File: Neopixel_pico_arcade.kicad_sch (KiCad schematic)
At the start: 14 parts

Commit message: Adds a buzzer to the schematics
We needed a way to generate some kind of annoying sound :)
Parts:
- added Q?: 2N7002, Package_TO_SOT_SMD:SOT-23, symbol Transistor_FET:2N7002
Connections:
- net +5V: now also BZ?.1 (-)
- net BUZZ: now also Q?.1 (G); no longer BZ?.1 (-)
- net GND: now also Q?.2 (S); no longer BZ?.2 (+)
- new net: BZ?.2 (+), Q?.3 (D)
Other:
- moved on the sheet: BZ?
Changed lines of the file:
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@@
     (stroke (width 0) (type solid) (color 0 0 0 0))
   )
-  (wire (pts (xy 233.68 38.1) (xy 237.49 38.1))
+  (wire (pts (xy 212.09 46.99) (xy 215.9 46.99))
     (stroke (width 0) (type default) (color 0 0 0 0))
   )
-  (wire (pts (xy 236.22 43.18) (xy 236.22 45.72))
+  (wire (pts (xy 223.52 25.4) (xy 223.52 30.48))
     (stroke (width 0) (type default) (color 0 0 0 0))
   )
-  (wire (pts (xy 237.49 43.18) (xy 236.22 43.18))
+  (wire (pts (xy 223.52 30.48) (xy 224.79 30.48))
+    (stroke (width 0) (type default) (color 0 0 0 0))
+  )
+  (wire (pts (xy 223.52 35.56) (xy 223.52 41.91))
+    (stroke (width 0) (type default) (color 0 0 0 0))
+  )
+  (wire (pts (xy 223.52 52.07) (xy 223.52 55.88))
+    (stroke (width 0) (type default) (color 0 0 0 0))
+  )
+  (wire (pts (xy 224.79 35.56) (xy 223.52 35.56))
     (stroke (width 0) (type default) (color 0 0 0 0))
   )
@@
     )
   )
-  (global_label "BUZZ" (shape input) (at 233.68 38.1 180) (fields_autoplaced)
+  (global_label "BUZZ" (shape input) (at 212.09 46.99 180) (fields_autoplaced)
     (effects (font (size 1.27 1.27)) (justify right))
-    (property "Intersheet References" "${INTERSHEET_REFS}" (id 0) (at 226.2474 38.1794 0)
+    (property "Intersheet References" "${INTERSHEET_REFS}" (id 0) (at 204.6574 47.0694 0)
       (effects (font (size 1.27 1.27)) (justify right) hide)
     )
@@
     (pin "1")
   )
+  (symbol (lib_id "Generative_picture:+5V_USB") (at 223.52 25.4 0) (unit 1)
+    (in_bom yes) (on_board yes)
+    (property "Reference" "#PWR?" (id 0) (at 223.52 29.21 0)
+      (effects (font (size 1.27 1.27)) hide)
+    )
+    (property "Value" "+5V" (id 1) (at 223.8883 21.0756 0))
+    (property "Footprint" "" (id 2) (at 223.52 25.4 0)
+      (effects (font (size 1.27 1.27)) hide)
+    )
+    (property "Datasheet" "" (id 3) (at 223.52 25.4 0)
+      (effects (font (size 1.27 1.27)) hide)
+    )
+    (pin "1")
+  )
   (symbol (lib_id "Generative_picture:+5V_USB") (at 240.665 64.77 0) (unit 1)
     (in_bom yes) (on_board yes)
@@
     (pin "1")
   )
-  (symbol (lib_id "power:GND") (at 236.22 45.72 0) (mirror y) (unit 1)
-    (in_bom yes) (on_board yes)
-    (property "Reference" "#PWR?" (id 0) (at 236.22 52.07 0)
-      (effects (font (size 1.27 1.27)) hide)
-    )
-    (property "Value" "GND" (id 1) (at 236.1057 50.0444 0))
-    (property "Footprint" "" (id 2) (at 236.22 45.72 0)
-      (effects (font (size 1.27 1.27)) hide)
-    )
-    (property "Datasheet" "" (id 3) (at 236.22 45.72 0)
+  (symbol (lib_id "power:GND") (at 223.52 55.88 0) (mirror y) (unit 1)
+    (in_bom yes) (on_board yes)
+    (property "Reference" "#PWR?" (id 0) (at 223.52 62.23 0)
+      (effects (font (size 1.27 1.27)) hide)
+    )
+    (property "Value" "GND" (id 1) (at 223.4057 60.2044 0))
+    (property "Footprint" "" (id 2) (at 223.52 55.88 0)
+      (effects (font (size 1.27 1.27)) hide)
+    )
+    (property "Datasheet" "" (id 3) (at 223.52 55.88 0)
       (effects (font (size 1.27 1.27)) hide)
     )
@@
     (pin "3")
   )
-  (symbol (lib_id "Device:Buzzer") (at 240.03 40.64 0) (unit 1)
+  (symbol (lib_id "Device:Buzzer") (at 227.33 33.02 0) (unit 1)
     (in_bom yes) (on_board yes) (fields_autoplaced)
-    (property "Reference" "BZ?" (id 0) (at 243.8401 39.7315 0)
+    (property "Reference" "BZ?" (id 0) (at 231.1401 32.1115 0)
       (effects (font (size 1.27 1.27)) (justify left))
     )
-    (property "Value" "Buzzer" (id 1) (at 243.8401 42.5066 0)
+    (property "Value" "Buzzer" (id 1) (at 231.1401 34.8866 0)
       (effects (font (size 1.27 1.27)) (justify left))
     )
-    (property "Footprint" "" (id 2) (at 239.395 38.1 90)
-      (effects (font (size 1.27 1.27)) hide)
-    )
-    (property "Datasheet" "~" (id 3) (at 239.395 38.1 90)
+    (property "Footprint" "" (id 2) (at 226.695 30.48 90)
+      (effects (font (size 1.27 1.27)) hide)
+    )
+    (property "Datasheet" "~" (id 3) (at 226.695 30.48 90)
       (effects (font (size 1.27 1.27)) hide)
     )
@@
     (pin "6")
     (pin "7")
+  )
+  (symbol (lib_id "Transistor_FET:2N7002") (at 220.98 46.99 0) (unit 1)
+    (in_bom yes) (on_board yes) (fields_autoplaced)
+    (property "Reference" "Q?" (id 0) (at 226.1871 46.0815 0)
+      (effects (font (size 1.27 1.27)) (justify left))
+    )
+    (property "Value" "2N7002" (id 1) (at 226.1871 48.8566 0)
+      (effects (font (size 1.27 1.27)) (justify left))
+    )
+    (property "Footprint" "Package_TO_SOT_SMD:SOT-23" (id 2) (at 226.06 48.895 0)
+      (effects (font (size 1.27 1.27) italic) (justify left) hide)
+    )
+    (property "Datasheet" "https://www.onsemi.com/pub/Collateral/NDS7002A-D.PDF" (id 3) (at 220.98 46.99 0)
+      (effects (font (size 1.27 1.27)) (justify left) hide)
+    )
+    (pin "1")
+    (pin "2")
+    (pin "3")
   )
   (symbol (lib_id "Logic_LevelTranslator:SN74LV1T34DBV") (at 185.42 99.06 0) (unit 1)
@@
       (reference "#PWR?") (unit 1) (value "GND") (footprint "")
     )
+    (path "/81137ea9-4a7e-4aeb-afc5-22a694c5b1ca"
+      (reference "#PWR?") (unit 1) (value "+5V") (footprint "")
+    )
     (path "/ed4fcb8f-53b7-458f-bfaa-4aa127051293/85aba269-7e69-4722-acf3-3e79713ac6fd"
       (reference "#PWR?") (unit 1) (value "+5V") (footprint "")
@@
       (reference "JP?") (unit 1) (value "jmp") (footprint "")
     )
+    (path "/691f88c6-2cd2-4539-9dfe-b9f1bc68fc22"
+      (reference "Q?") (unit 1) (value "2N7002") (footprint "Package_TO_SOT_SMD:SOT-23")
+    )
     (path "/0885f3bc-cb16-420f-8579-461f1e11360e"

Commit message: Annotates components on schematics
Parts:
- gave numbers to parts that had none: 15

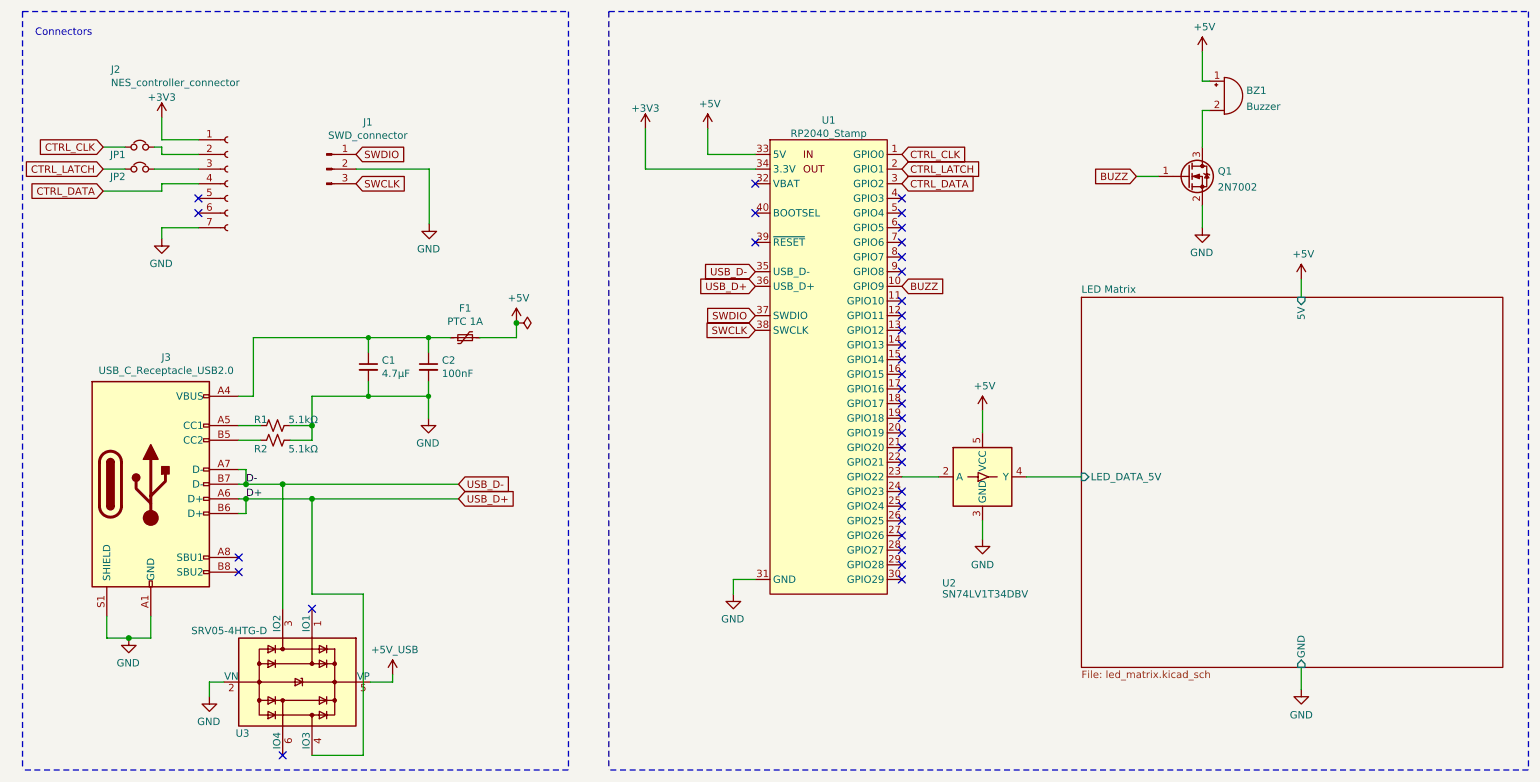
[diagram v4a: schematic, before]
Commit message: Align elements to grid
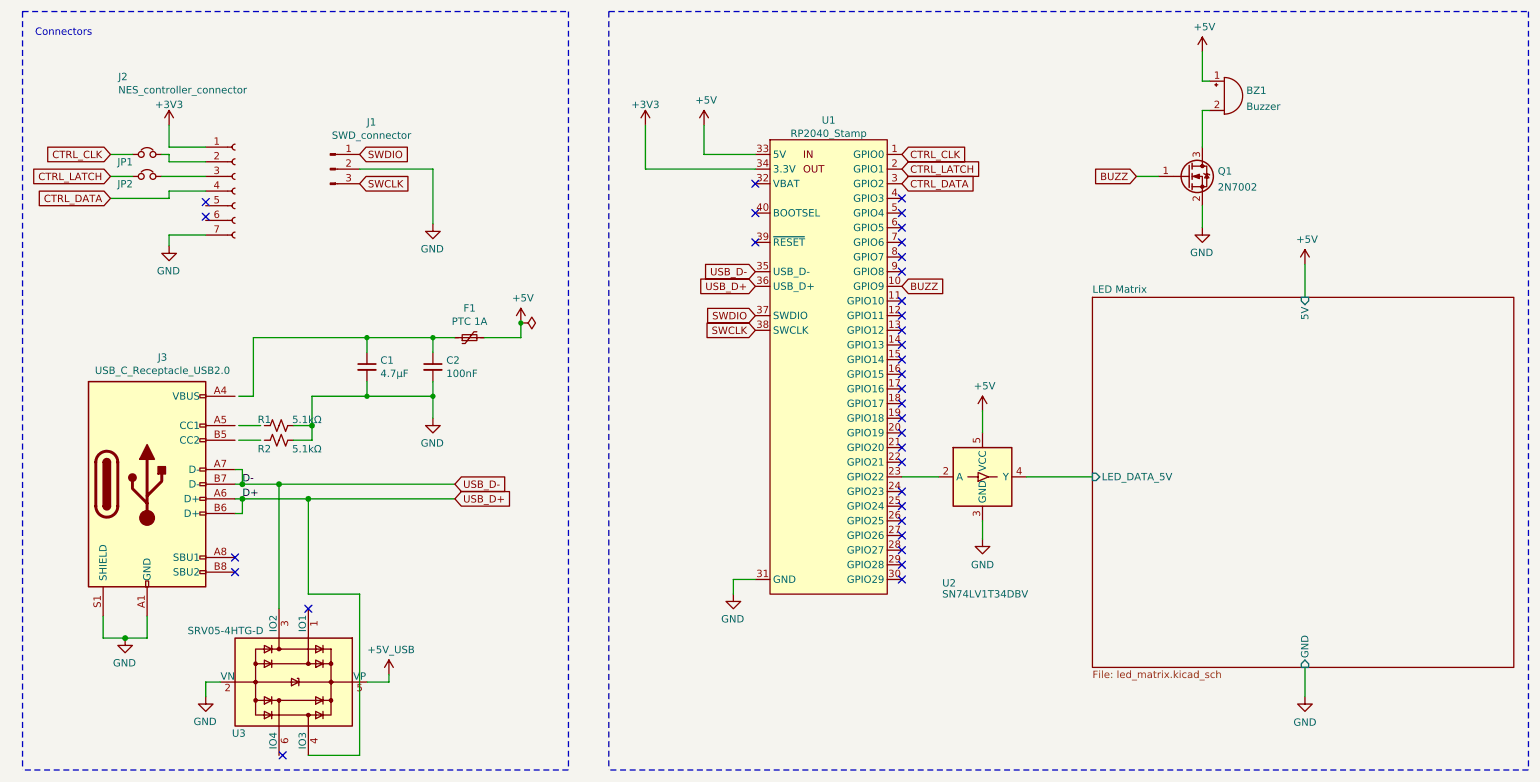
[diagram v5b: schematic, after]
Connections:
- net at R1.1: no longer J3.A5 (CC1)
- net at J3.A4 (VBUS), J3.A9 (VBUS), J3.B4 (VBUS)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: no longer C1.1, C2.1, F1.1
- net at J3.B5 (CC2): no longer R2.1
- new net: C1.1, C2.1, F1.1
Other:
- moved on the sheet: C2, F1, J1, J2, J3, JP1, JP2, R1, R2, U3

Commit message: Changes +5v symbols
These were copied from another project and Kicad included references to
that library.
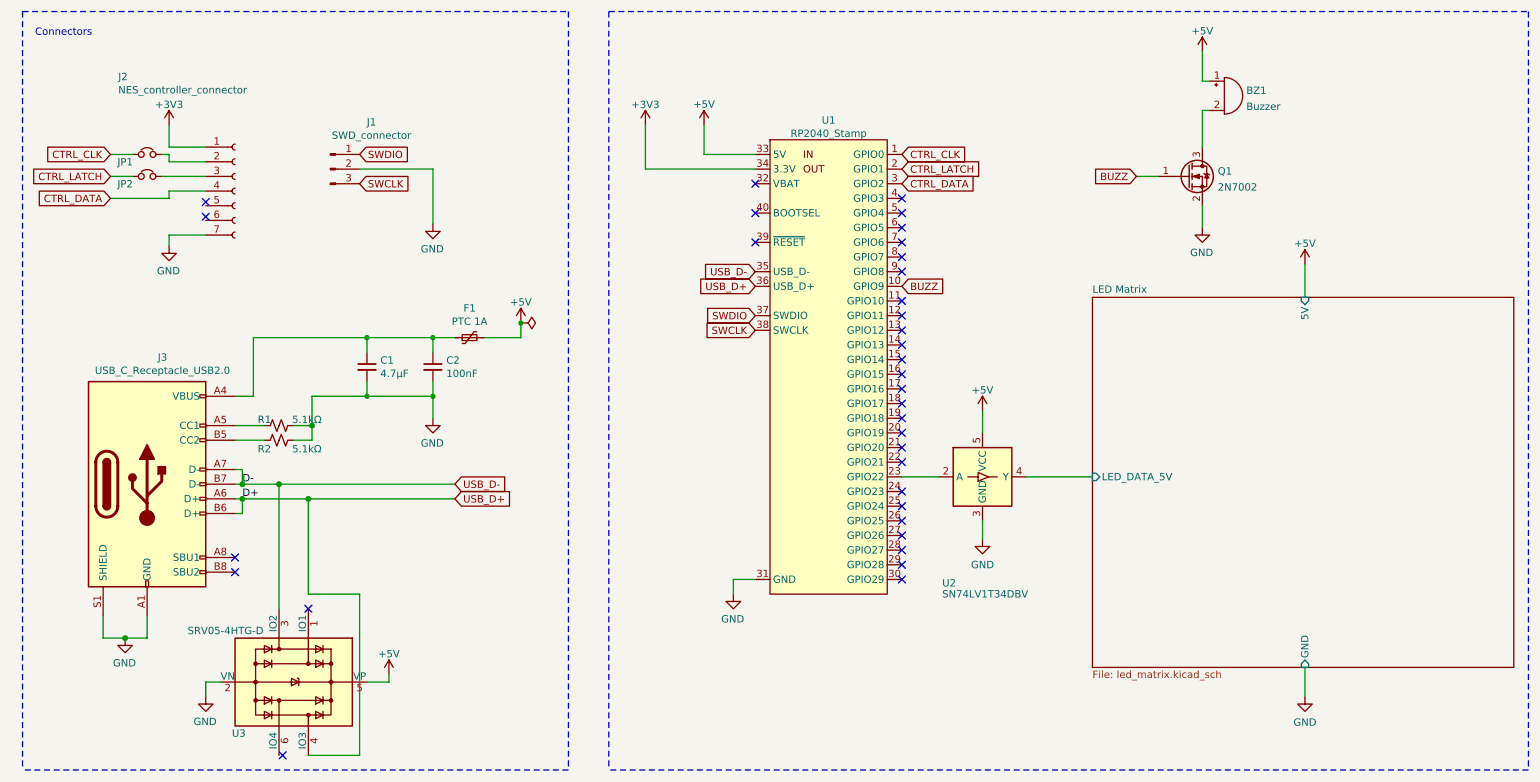
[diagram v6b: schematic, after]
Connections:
- net at R1.1: now also J3.A5 (CC1)
- net at C1.1, C2.1, F1.1: now also J3.A4 (VBUS), J3.A9 (VBUS), J3.B4 (VBUS), J3.B9 (VBUS)
- net at J3.B5 (CC2): now also R2.1
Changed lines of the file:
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@@
     (stroke (width 0) (type default) (color 0 0 0 0))
+  )
+  (wire (pts (xy 55.88 85.09) (xy 59.055 85.09))
+    (stroke (width 0) (type solid) (color 0 0 0 0))
+  )
+  (wire (pts (xy 55.88 90.17) (xy 60.96 90.17))
+    (stroke (width 0) (type solid) (color 0 0 0 0))
+  )
+  (wire (pts (xy 55.88 92.71) (xy 60.96 92.71))
+    (stroke (width 0) (type solid) (color 0 0 0 0))
   )
   (wire (pts (xy 55.88 97.79) (xy 57.15 97.79))
@@
   )
   (wire (pts (xy 55.88 105.41) (xy 57.15 105.41))
-    (stroke (width 0) (type solid) (color 0 0 0 0))
-  )
-  (wire (pts (xy 56.515 85.09) (xy 59.055 85.09))
-    (stroke (width 0) (type solid) (color 0 0 0 0))
-  )
-  (wire (pts (xy 56.515 90.17) (xy 60.325 90.17))
-    (stroke (width 0) (type solid) (color 0 0 0 0))
-  )
-  (wire (pts (xy 56.515 92.71) (xy 60.325 92.71))
     (stroke (width 0) (type solid) (color 0 0 0 0))
   )
@@
     (pin "1")
   )
-  (symbol (lib_id "Generative_picture:+5V_USB") (at 82.55 133.35 0) (unit 1)
-    (in_bom yes) (on_board yes)
-    (property "Reference" "#PWR015" (id 0) (at 82.55 137.16 0)
-      (effects (font (size 1.27 1.27)) hide)
-    )
-    (property "Value" "+5V_USB" (id 1) (at 82.9183 129.0256 0))
+  (symbol (lib_id "power:+5V") (at 82.55 133.35 0) (unit 1)
+    (in_bom yes) (on_board yes) (fields_autoplaced)
+    (property "Reference" "#PWR?" (id 0) (at 82.55 137.16 0)
+      (effects (font (size 1.27 1.27)) hide)
+    )
+    (property "Value" "+5V" (id 1) (at 82.55 129.7454 0))
     (property "Footprint" "" (id 2) (at 82.55 133.35 0)
       (effects (font (size 1.27 1.27)) hide)
@@
     (pin "1")
   )
-  (symbol (lib_id "Generative_picture:+5V_USB") (at 105.41 72.39 0) (unit 1)
-    (in_bom yes) (on_board yes)
-    (property "Reference" "#PWR09" (id 0) (at 105.41 76.2 0)
-      (effects (font (size 1.27 1.27)) hide)
-    )
-    (property "Value" "+5V" (id 1) (at 105.7783 68.0656 0))
+  (symbol (lib_id "power:+5V") (at 105.41 72.39 0) (unit 1)
+    (in_bom yes) (on_board yes) (fields_autoplaced)
+    (property "Reference" "#PWR?" (id 0) (at 105.41 76.2 0)
+      (effects (font (size 1.27 1.27)) hide)
+    )
+    (property "Value" "+5V" (id 1) (at 105.41 68.7854 0))
     (property "Footprint" "" (id 2) (at 105.41 72.39 0)
       (effects (font (size 1.27 1.27)) hide)
@@
     (pin "1")
   )
-  (symbol (lib_id "Generative_picture:+5V_USB") (at 137.16 38.1 0) (unit 1)
-    (in_bom yes) (on_board yes)
-    (property "Reference" "#PWR04" (id 0) (at 137.16 41.91 0)
-      (effects (font (size 1.27 1.27)) hide)
-    )
-    (property "Value" "+5V" (id 1) (at 137.5283 33.7756 0))
+  (symbol (lib_id "power:+5V") (at 137.16 38.1 0) (unit 1)
+    (in_bom yes) (on_board yes) (fields_autoplaced)
+    (property "Reference" "#PWR?" (id 0) (at 137.16 41.91 0)
+      (effects (font (size 1.27 1.27)) hide)
+    )
+    (property "Value" "+5V" (id 1) (at 137.16 34.4954 0))
     (property "Footprint" "" (id 2) (at 137.16 38.1 0)
       (effects (font (size 1.27 1.27)) hide)
@@
     (pin "1")
   )
-  (symbol (lib_id "Generative_picture:+5V_USB") (at 185.42 87.63 0) (unit 1)
-    (in_bom yes) (on_board yes)
-    (property "Reference" "#PWR010" (id 0) (at 185.42 91.44 0)
-      (effects (font (size 1.27 1.27)) hide)
-    )
-    (property "Value" "+5V" (id 1) (at 185.7883 83.3056 0))
+  (symbol (lib_id "power:+5V") (at 185.42 87.63 0) (unit 1)
+    (in_bom yes) (on_board yes) (fields_autoplaced)
+    (property "Reference" "#PWR?" (id 0) (at 185.42 91.44 0)
+      (effects (font (size 1.27 1.27)) hide)
+    )
+    (property "Value" "+5V" (id 1) (at 185.42 84.0254 0))
     (property "Footprint" "" (id 2) (at 185.42 87.63 0)
       (effects (font (size 1.27 1.27)) hide)
@@
     (pin "1")
   )
-  (symbol (lib_id "Generative_picture:+5V_USB") (at 223.52 25.4 0) (unit 1)
-    (in_bom yes) (on_board yes)
-    (property "Reference" "#PWR01" (id 0) (at 223.52 29.21 0)
-      (effects (font (size 1.27 1.27)) hide)
-    )
-    (property "Value" "+5V" (id 1) (at 223.8883 21.0756 0))
+  (symbol (lib_id "power:+5V") (at 223.52 25.4 0) (unit 1)
+    (in_bom yes) (on_board yes) (fields_autoplaced)
+    (property "Reference" "#PWR?" (id 0) (at 223.52 29.21 0)
+      (effects (font (size 1.27 1.27)) hide)
+    )
+    (property "Value" "+5V" (id 1) (at 223.52 21.7954 0))
     (property "Footprint" "" (id 2) (at 223.52 25.4 0)
       (effects (font (size 1.27 1.27)) hide)
@@
     (pin "1")
   )
-  (symbol (lib_id "Generative_picture:+5V_USB") (at 241.3 62.23 0) (unit 1)
-    (in_bom yes) (on_board yes)
-    (property "Reference" "#PWR08" (id 0) (at 241.3 66.04 0)
-      (effects (font (size 1.27 1.27)) hide)
-    )
-    (property "Value" "+5V" (id 1) (at 241.6683 57.9056 0))
+  (symbol (lib_id "power:+5V") (at 241.3 62.23 0) (unit 1)
+    (in_bom yes) (on_board yes) (fields_autoplaced)
+    (property "Reference" "#PWR?" (id 0) (at 241.3 66.04 0)
+      (effects (font (size 1.27 1.27)) hide)
+    )
+    (property "Value" "+5V" (id 1) (at 241.3 58.6254 0))
     (property "Footprint" "" (id 2) (at 241.3 62.23 0)
       (effects (font (size 1.27 1.27)) hide)
@@
       (reference "#FLG01") (unit 1) (value "PWR_FLAG") (footprint "")
     )
-    (path "/81137ea9-4a7e-4aeb-afc5-22a694c5b1ca"
-      (reference "#PWR01") (unit 1) (value "+5V") (footprint "")
-    )
     (path "/1729631f-de18-4c58-a71d-335612619424"
       (reference "#PWR02") (unit 1) (value "+3V3") (footprint "")
@@
       (reference "#PWR03") (unit 1) (value "+3V3") (footprint "")
     )
-    (path "/8ff9f093-81ea-42b2-82f0-cf43f6906b37"
-      (reference "#PWR04") (unit 1) (value "+5V") (footprint "")
-    )
     (path "/1556db3c-27c0-41bc-8714-1a11047a4079"
       (reference "#PWR05") (unit 1) (value "GND") (footprint "")
@@
       (reference "#PWR07") (unit 1) (value "GND") (footprint "")
     )
-    (path "/6a4bb6a6-fea8-401e-9d2b-19300508e457"
-      (reference "#PWR08") (unit 1) (value "+5V") (footprint "")
-    )
-    (path "/4f1fe51c-79e1-410a-ae57-948c663e40fc"
-      (reference "#PWR09") (unit 1) (value "+5V") (footprint "")
-    )
-    (path "/defb1518-fb9b-4034-871f-ab51c6073e63"
-      (reference "#PWR010") (unit 1) (value "+5V") (footprint "")
-    )
     (path "/c7debda7-ea54-4d5a-893a-d932ed8e0f8e"
       (reference "#PWR011") (unit 1) (value "GND") (footprint "")
@@
       (reference "#PWR014") (unit 1) (value "GND") (footprint "")
     )
-    (path "/74b6e856-17de-4926-93b2-1018d6a5ffce"
-      (reference "#PWR015") (unit 1) (value "+5V_USB") (footprint "")
-    )
     (path "/60d49c71-aeb1-4fc7-ab52-02d624e44468"
       (reference "#PWR016") (unit 1) (value "GND") (footprint "")
@@
       (reference "#PWR0147") (unit 1) (value "GND") (footprint "")
     )
+    (path "/2d959cc5-b271-4536-9ea7-f39ea9c51a26"
+      (reference "#PWR?") (unit 1) (value "+5V") (footprint "")
+    )
+    (path "/31716d8f-df2f-4a2f-94b3-681ba3d75057"
+      (reference "#PWR?") (unit 1) (value "+5V") (footprint "")
+    )
+    (path "/6c49b017-7d26-4b31-9203-f7fa6b2a453a"
+      (reference "#PWR?") (unit 1) (value "+5V") (footprint "")
+    )
+    (path "/a1b8871f-612b-4d6e-b819-9768d829e3c8"
+      (reference "#PWR?") (unit 1) (value "+5V") (footprint "")
+    )
+    (path "/b58d9025-f559-43a2-8cad-d24d15fa24bc"
+      (reference "#PWR?") (unit 1) (value "+5V") (footprint "")
+    )
+    (path "/f5948381-d08e-4743-abc3-ccc0a0ba9733"
+      (reference "#PWR?") (unit 1) (value "+5V") (footprint "")
+    )
     (path "/6b2c05fc-325d-47a8-82b6-bd0eb739f2e9"
